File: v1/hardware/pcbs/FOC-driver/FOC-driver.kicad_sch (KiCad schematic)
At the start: 146 parts, among them J10 S4B-XH-A, J11 S10B-XH-A, J12 S8B-XH-A, J13 S5B-XH-A, J14 S2B-XH-A, J15 S5B-XH-A, J16 S2B-XH-A, J2 HB9500-3, J3 B2B-XH-A, J4 B2B-XH-A, J5 B2B-XH-A, J6 B2B-XH-A, J7 S2B-XH-A, J8 S5B-XH-A, J9 S4B-XH-A, Q10 40N05, Q11 40N05, Q8 40N05, Q9 40N05, SW1 TS-1088-AR02016, SW2 MSK22D18G2 125, Y1 C19674287, Y2 C48615

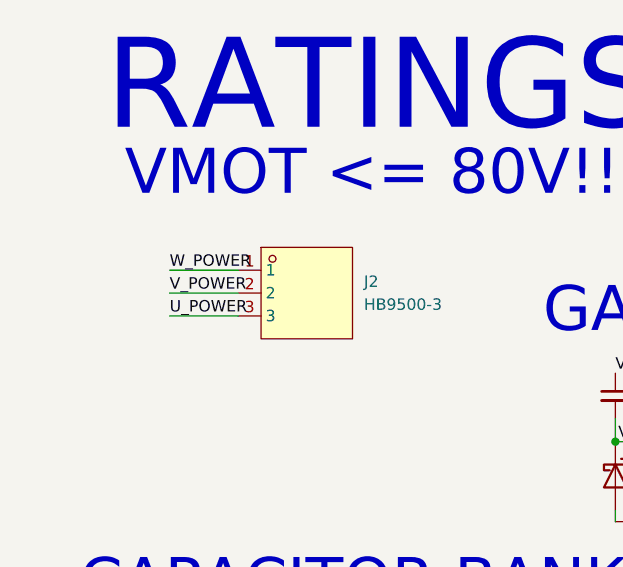
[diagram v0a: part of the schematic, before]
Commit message: new FOC driver inverter out label
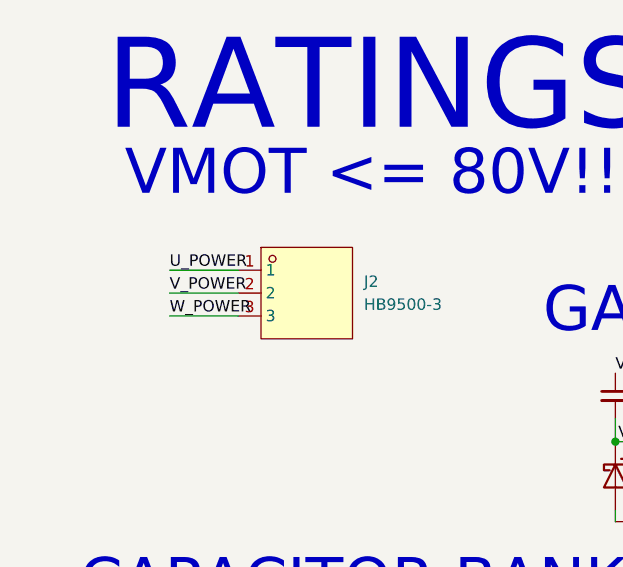
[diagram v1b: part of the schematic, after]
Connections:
- net U_POWER: now also J2.1; no longer J2.3
- net W_POWER: now also J2.3; no longer J2.1
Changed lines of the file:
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@@
 	(wire
 		(pts
+			(xy 24.13 53.34) (xy 31.75 53.34)
+		)
+		(stroke
+			(width 0)
+			(type default)
+		)
+	)
+	(wire
+		(pts
 			(xy 416.56 281.94) (xy 416.56 287.02)
 		)
@@
 	(wire
 		(pts
-			(xy 24.13 48.26) (xy 31.75 48.26)
-		)
-		(stroke
-			(width 0)
-			(type default)
-		)
-	)
-	(wire
-		(pts
 			(xy 466.09 48.26) (xy 463.55 48.26)
 		)
@@
 	(wire
 		(pts
+			(xy 24.13 48.26) (xy 31.75 48.26)
+		)
+		(stroke
+			(width 0)
+			(type default)
+		)
+	)
+	(wire
+		(pts
 			(xy 284.48 340.36) (xy 297.18 340.36)
 		)
@@
 		)
 	)
-	(wire
-		(pts
-			(xy 24.13 53.34) (xy 31.75 53.34)
-		)
-		(stroke
-			(width 0)
-			(type default)
-		)
-	)
 	(label "W_HIGH_GATE"
 		(at 191.77 91.44 0)
@@
 		)
 	)
+	(label "U_POWER"
+		(at 24.13 48.26 0)
+		(effects
+			(font
+				(size 1.27 1.27)
+			)
+			(justify left bottom)
+		)
+	)
 	(label "ENC_DIFF.B-"
 		(at 209.55 340.36 180)
@@
 		)
 	)
-	(label "W_POWER"
-		(at 24.13 48.26 0)
-		(effects
-			(font
-				(size 1.27 1.27)
-			)
-			(justify left bottom)
-		)
-	)
 	(label "ENC.A"
 		(at 430.53 95.25 0)
@@
 		)
 	)
-	(label "U_POWER"
-		(at 24.13 53.34 0)
-		(effects
-			(font
-				(size 1.27 1.27)
-			)
-			(justify left bottom)
-		)
-	)
 	(label "DEBUG{SWCLK SWDIO SWO}"
 		(at 387.35 134.62 180)
@@
 		)
 	)
+	(label "W_POWER"
+		(at 24.13 53.34 0)
+		(effects
+			(font
+				(size 1.27 1.27)
+			)
+			(justify left bottom)
+		)
+	)

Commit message: new FOC driver done
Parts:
- removed C31: 100nF 50V, Capacitor_SMD:C_0402_1005Metric, symbol symbols:C_Small
- removed C32: 1uF 16V, Capacitor_SMD:C_0402_1005Metric, symbol symbols:C_Small
- removed C4: 820uF 100V (C443165), Capacitor_THT:C_Radial_D18.0mm_H35.5mm_P7.50mm, symbol symbols:C_Polarized
- removed R4: 4.7K, Resistor_SMD:R_0402_1005Metric, symbol symbols:R_Small
- removed R5: 1K, Resistor_SMD:R_0402_1005Metric, symbol symbols:R_Small
- removed TH1, TH2, TH3, TH4, TH5, TH6: NCP15XH103F03RC, Resistor_SMD:R_0402_1005Metric, symbol Device:Thermistor
- removed TP17: TestPoint, Connector_PinSocket_2.54mm:PinSocket_1x01_P2.54mm_Vertical, symbol symbols:TestPoint
- added C70: 100nF 50V, Capacitor_SMD:C_0402_1005Metric, symbol symbols:C_Small
- added J17, J18, J19, J20, J21, J22: B2B-XH-A, Connector_JST:JST_XH_B2B-XH-A_1x02_P2.50mm_Vertical, symbol Connector_Generic:Conn_01x02
- added R68, R69, R70, R71, R72, R73, R74: 10K, Resistor_SMD:R_0402_1005Metric, symbol symbols:R_Small
- added R75, R76: 100, Resistor_SMD:R_0402_1005Metric, symbol symbols:R_Small
- added TP8: PinHeader 1x1, Connector_PinHeader_2.54mm:PinHeader_1x01_P2.54mm_Vertical, symbol symbols:TestPoint
- TP1, TP2, TP3, TP4, TP5, TP6, TP7: value TestPoint -> PinHeader 1x1; footprint Connector_PinSocket_2.54mm:PinSocket_1x01_P2.54mm_Vertical -> Connector_PinHeader_2.54mm:PinHeader_1x01_P2.54mm_Vertical
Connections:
- net 5V_SENSE is gone; now on net U_HIGH_TEMP: MCU1.13 (PA1)
- net VS1 is gone; now on net W_POWER: C9.1, GDRV1.18 (VS1)
- net VS2 is gone; now on net V_POWER: C10.1, GDRV1.15 (VS2)
- net VS3 is gone; now on net U_POWER: C11.1, GDRV1.12 (VS3)
- net +12V: now also TP6.1, C70.2; no longer TP5.1
- net +3.3V: now also J17.1 (Pin_1), J18.1 (Pin_1), J19.1 (Pin_1), J20.1 (Pin_1), J21.1 (Pin_1), J22.1 (Pin_1), TP8.1
- net +5V: now also TP7.1
- net 12V_SENSE: now also MCU1.17 (PA3); no longer MCU1.12 (PA0)
- net DEBUG.SWDIO: now also J15.2 (Pin_2); no longer J15.4 (Pin_4)
- net DEBUG.SWO: now also J15.4 (Pin_4); no longer J15.5 (Pin_5)
- net DIP.CONF0: now also MCU1.54 (PC12); no longer MCU1.30 (PB10)
- net DIP.CONF1: now also MCU1.53 (PC11); no longer MCU1.33 (PB11)
- net DIP.CONF2: now also MCU1.52 (PC10); no longer MCU1.34 (PB12)
- net ENC.SCS: now also MCU1.26 (PB2); no longer MCU1.37 (PB15)
- net ENDSTOP1: now also MCU1.62 (PB9); no longer MCU1.8 (PC0)
- net ENDSTOP1+: now also R75.1
- net ENDSTOP1-: now also R75.2
- net ENDSTOP2: now also MCU1.8 (PC0); no longer MCU1.62 (PB9)
- net ENDSTOP2+: now also R76.1
- net ENDSTOP2-: now also R76.2
- net FAN1.EN: now also MCU1.37 (PB15); no longer MCU1.26 (PB2)
- net FAN1.PWM: now also MCU1.41 (PC9); no longer MCU1.51 (PA15)
- net FAN2.EN: now also MCU1.34 (PB12); no longer MCU1.54 (PC12)
- net FAN2.PWM: now also MCU1.40 (PC8); no longer MCU1.39 (PC7)
- net FAN3.EN: now also MCU1.33 (PB11); no longer MCU1.53 (PC11)
- net FAN3.PWM: now also MCU1.39 (PC7); no longer MCU1.40 (PC8)
- net FAN4.EN: now also MCU1.30 (PB10); no longer MCU1.52 (PC10)
- net FAN4.PWM: now also MCU1.51 (PA15); no longer MCU1.41 (PC9)
- net FDCAN.CAN+: now also J8.3 (Pin_3), J8.4 (Pin_4), SW2.3; no longer J8.2 (Pin_2), J8.5 (Pin_5), SW2.2
- net FDCAN.CAN-: now also J8.2 (Pin_2), J8.5 (Pin_5), SW2.6; no longer J8.3 (Pin_3), J8.4 (Pin_4), SW2.5
- net GND: now also SW2.1, SW2.4, C70.1, R68.2, R69.2, R70.2, R71.2, R72.2, R73.2, R74.2; no longer TP7.1
- net MOTOR_TEMP: now also MCU1.20 (PA6)
- net NRST: now also J15.5 (Pin_5); no longer J15.2 (Pin_2)
- net RS422.RX+: now also J13.3 (Pin_3); no longer J13.4 (Pin_4)
- net RS422.RX-: now also J13.2 (Pin_2); no longer J13.5 (Pin_5)
- net RS422.TX+: now also J13.5 (Pin_5); no longer J13.2 (Pin_2)
- net RS422.TX-: now also J13.4 (Pin_4); no longer J13.3 (Pin_3)
- net U_HIGH_GATE: now also GDRV1.13 (HO3); no longer GDRV1.19 (HO1)
- net U_HIGH_PWM: now also GDRV1.24 (HIN3), MCU1.44 (PA10); no longer GDRV1.22 (HIN1), MCU1.42 (PA8)
- net U_HIGH_TEMP: now also J17.2 (Pin_2); no longer MCU1.14 (PA2)
- net U_LOW_GATE: now also GDRV1.9 (LO3); no longer GDRV1.11 (LO1)
- net U_LOW_PWM: now also GDRV1.3 (LIN3), MCU1.25 (PB1); no longer GDRV1.1 (LIN1), MCU1.2 (PC13)
- net U_LOW_TEMP: now also MCU1.14 (PA2), J18.2 (Pin_2); no longer MCU1.17 (PA3)
- net VMOT: now also TP5.1; no longer TP6.1
- net VMOT_SENSE: now also MCU1.22 (PC4); no longer MCU1.20 (PA6)
- net V_HIGH_TEMP: now also MCU1.11 (PC3), J19.2 (Pin_2); no longer MCU1.9 (PC1)
- net V_LOW_TEMP: now also MCU1.12 (PA0), J20.2 (Pin_2); no longer MCU1.10 (PC2)
- net W_HIGH_GATE: now also GDRV1.19 (HO1); no longer GDRV1.13 (HO3)
- net W_HIGH_PWM: now also GDRV1.22 (HIN1), MCU1.42 (PA8); no longer GDRV1.24 (HIN3), MCU1.44 (PA10)
- net W_HIGH_TEMP: now also MCU1.9 (PC1), J21.2 (Pin_2); no longer MCU1.11 (PC3)
- net W_LOW_GATE: now also GDRV1.11 (LO1); no longer GDRV1.9 (LO3)
- net W_LOW_PWM: now also GDRV1.1 (LIN1), MCU1.2 (PC13); no longer GDRV1.3 (LIN3), MCU1.25 (PB1)
- net W_LOW_TEMP: now also MCU1.10 (PC2), J22.2 (Pin_2); no longer MCU1.22 (PC4)
- net CANTERM_MID: now reaches C41.2, R35.1, R36.1
- net CANTERM+: now reaches R35.2
- net CANTERM+: now also SW2.2; no longer SW2.6
- net at DIFF_RECV1.4 (DI): now also R70.1
- net at DIFF_RECV6.4 (DI): now also R73.1
- net at DIFF_RECV2.4 (DI): now also R71.1
- net at DIFF_RECV4.4 (DI): now also R72.1
- net at DIFF_RECV5.4 (DI): now also R68.1
- net at DIFF_RECV7.4 (DI): now also R74.1
- net CANTERM-: now reaches R36.2
- net CANTERM-: now also SW2.5; no longer SW2.3
- net at DIFF_RECV3.4 (DI): now also R69.1
- no-connect marks 24 -> 15
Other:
- note added: "INVERTER: U_HIGH_PWM: TIM1_CH3 (PA10)r U_LOW_PWM: TIM1_CH3N (PB1) W_HIGH_PWM: TIM1_CH1 (PA8) W_LOW_PWM: TIM1_CH1N (PC13) V_HIGH_PWM: TIM1_CH2 (PA9) V_LOW_PWM: TIM1_CH2N (PB0) CURRENT SENSING: U_I_SENSE: OPAMP1_VINP => ADC1_IN13 (PA7) V_I_SENSE: OPAMP2_VINP => ADC2_IN16 (PB14) W_I_SENSE: OPAMP3_VINP => ADC1_IN12 (PB13) VOLTAGE SENSING: VMOT_SENSE: ADC2_IN5 (PC4) 12V_SENSE: ADC1_IN4 (PA3) TEMPERATU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"
- note added: "TESTPOINTS"
- note removed: "INVERTER: U_HIGH_PWM: TIM1_CH1 (PA8) U_LOW_PWM: TIM1_CH1N (PC13) V_HIGH_PWM: TIM1_CH2 (PA9) V_LOW_PWM: TIM1_CH2N (PB0) W_HIGH_PWM: TIM1_CH3 (PA10) W_LOW_PWM: TIM1_CH3N (PB1) CURRENT SENSING: U_I_SENSE: OPAMP1_VINP => ADC1_IN13 (PA7) V_I_SENSE: OPAMP2_VINP => ADC2_IN16 (PB14) W_I_SENSE: OPAMP3_VINP => ADC1_IN12 (PB13) VOLTAGE SENSING: VMOT_SENSE: ADC2_IN3 (PA6) 12V_SENSE: ADC1_IN1 (PA0) 5V_SENSE: 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"
- moved on the sheet: C10, C11, C17, C39, C41, C9, D1, D2, D3, FDCAN_TSCV1, J10, J8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

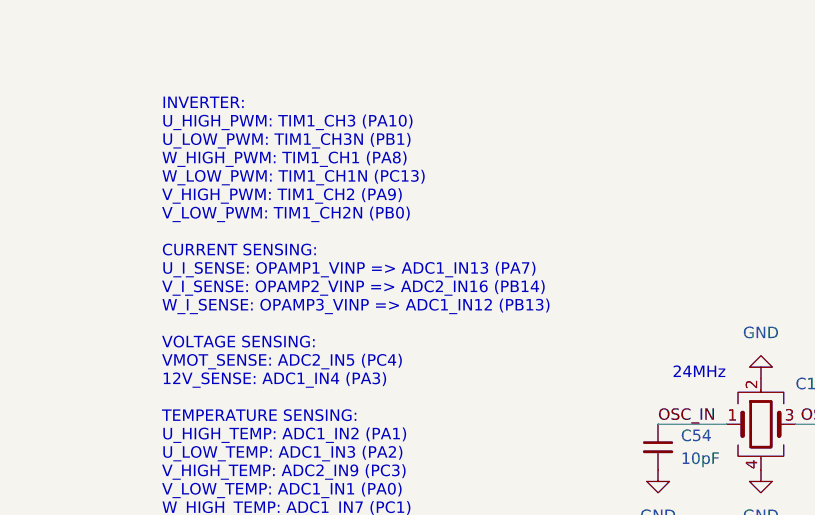
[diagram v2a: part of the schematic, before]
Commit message: corrected some pinouts
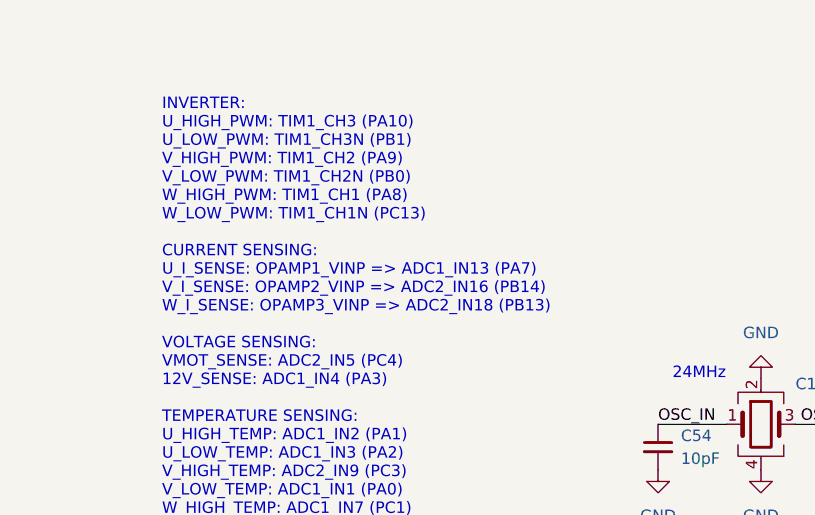
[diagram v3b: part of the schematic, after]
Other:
- note added: "INVERTER: U_HIGH_PWM: TIM1_CH3 (PA10)r U_LOW_PWM: TIM1_CH3N (PB1) V_HIGH_PWM: TIM1_CH2 (PA9)r V_LOW_PWM: TIM1_CH2N (PB0) W_HIGH_PWM: TIM1_CH1 (PA8) W_LOW_PWM: TIM1_CH1N (PC13) CURRENT SENSING: U_I_SENSE: OPAMP1_VINP => ADC1_IN13 (PA7) V_I_SENSE: OPAMP2_VINP => ADC2_IN16 (PB14) W_I_SENSE: OPAMP3_VINP => ADC2_IN18 (PB13) VOLTAGE SENSING: VMOT_SENSE: ADC2_IN5 (PC4) 12V_SENSE: ADC1_IN4 (PA3) TEMPERAT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"
- note removed: "INVERTER: U_HIGH_PWM: TIM1_CH3 (PA10)r U_LOW_PWM: TIM1_CH3N (PB1) W_HIGH_PWM: TIM1_CH1 (PA8) W_LOW_PWM: TIM1_CH1N (PC13) V_HIGH_PWM: TIM1_CH2 (PA9) V_LOW_PWM: TIM1_CH2N (PB0) CURRENT SENSING: U_I_SENSE: OPAMP1_VINP => ADC1_IN13 (PA7) V_I_SENSE: OPAMP2_VINP => ADC2_IN16 (PB14) W_I_SENSE: OPAMP3_VINP => ADC1_IN12 (PB13) VOLTAGE SENSING: VMOT_SENSE: ADC2_IN5 (PC4) 12V_SENSE: ADC1_IN4 (PA3) TEMPERATU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"
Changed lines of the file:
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@@
 		)
 	)
-	(text "INVERTER:\nU_HIGH_PWM: TIM1_CH3 (PA10)\r\nU_LOW_PWM: TIM1_CH3N (PB1)\nW_HIGH_PWM: TIM1_CH1 (PA8)\nW_LOW_PWM: TIM1_CH1N (PC13)\nV_HIGH_PWM: TIM1_CH2 (PA9)\nV_LOW_PWM: TIM1_CH2N (PB0)\n\nCURRENT SENSING:\nU_I_SENSE: OPAMP1_VINP => ADC1_IN13 (PA7)\nV_I_SENSE: OPAMP2_VINP => ADC2_IN16 (PB14)\nW_I_SENSE: OPAMP3_VINP => ADC1_IN12 (PB13)\n\nVOLTAGE SENSING:\nVMOT_SENSE: ADC2_IN5 (PC4)\n12V_SENSE: ADC1_IN4 (PA3)\n\nTEMPERATURE SENSING:\nU_HIGH_TEMP: ADC1_IN2 (PA1)\nU_LOW_TEMP: ADC1_IN3 (PA2)\nV_HIGH_TEMP: ADC2_IN9 (PC3)\nV_LOW_TEMP: ADC1_IN1 (PA0)\nW_HIGH_TEMP: ADC1_IN7 (PC1)\nW_LOW_TEMP: ADC1_IN8 (PC2)\nMOTOR_TEMP: ADC2_IN3 (PA6)\n\nFANS:\nFAN1_PWM: TIM8_CH4 (PC9)\r\nFAN1_EN: PB15\r\nFAN2_PWM: TIM8_CH3 (PC8)\r\nFAN2_EN: PB12\r\nFAN3_PWM: TIM8_CH2 (PC7)\r\nFAN3_EN: PB11\nFAN4_PWM: TIM8_CH1 (PA15)\nFAN4_EN: PB10\n\nDEBUG:\nSWCLK: PA14\nSWDIO: PA13\nSWO: PB3\nLED: PD2\n\nFDCAN:\nRX: FDCAN1_RX (PA11)\nTX: FDCAN1_TX (PA12)\n\nRS422:\nRX: USART1_RX (PB7)\nTX: USART1_TX (PB6)\n\nENCODER:\nSCLK: SPI1_SCLK (PA5)\nMISO: SPI1_MISO (PB4)\r\nMOSI: SPI1_MOSI (PB5)\nSCS: PB2\nA: TIM3_CH1 (PC6)\nB: TIM3_CH2 (PA4)\nZ: PC5\n\nENDSTOP:\nENDSTOP1: PB9\nENDSTOP2: PC0\n\nCONFIG:\nBOOT: BOOT0 (PB8)\nCONF1: PC12\nCONF2: PC11\nCONF3: PC10"
+	(text "INVERTER:\nU_HIGH_PWM: TIM1_CH3 (PA10)\r\nU_LOW_PWM: TIM1_CH3N (PB1)\nV_HIGH_PWM: TIM1_CH2 (PA9)\r\nV_LOW_PWM: TIM1_CH2N (PB0)\nW_HIGH_PWM: TIM1_CH1 (PA8)\nW_LOW_PWM: TIM1_CH1N (PC13)\n\nCURRENT SENSING:\nU_I_SENSE: OPAMP1_VINP => ADC1_IN13 (PA7)\nV_I_SENSE: OPAMP2_VINP => ADC2_IN16 (PB14)\nW_I_SENSE: OPAMP3_VINP => ADC2_IN18 (PB13)\n\nVOLTAGE SENSING:\nVMOT_SENSE: ADC2_IN5 (PC4)\n12V_SENSE: ADC1_IN4 (PA3)\n\nTEMPERATURE SENSING:\nU_HIGH_TEMP: ADC1_IN2 (PA1)\nU_LOW_TEMP: ADC1_IN3 (PA2)\nV_HIGH_TEMP: ADC2_IN9 (PC3)\nV_LOW_TEMP: ADC1_IN1 (PA0)\nW_HIGH_TEMP: ADC1_IN7 (PC1)\nW_LOW_TEMP: ADC1_IN8 (PC2)\nMOTOR_TEMP: ADC2_IN3 (PA6)\n\nFANS:\nFAN1_PWM: TIM8_CH4 (PC9)\r\nFAN1_EN: PB15\r\nFAN2_PWM: TIM8_CH3 (PC8)\r\nFAN2_EN: PB12\r\nFAN3_PWM: TIM8_CH2 (PC7)\r\nFAN3_EN: PB11\nFAN4_PWM: TIM8_CH1 (PA15)\nFAN4_EN: PB10\n\nDEBUG:\nSWCLK: PA14\nSWDIO: PA13\nSWO: PB3\nLED: PD2\n\nFDCAN:\nRX: FDCAN1_RX (PA11)\nTX: FDCAN1_TX (PA12)\n\nRS422:\nRX: USART1_RX (PB7)\nTX: USART1_TX (PB6)\n\nENCODER:\nSCLK: SPI1_SCLK (PA5)\nMISO: SPI1_MISO (PB4)\r\nMOSI: SPI1_MOSI (PB5)\nSCS: PB2\nA: TIM3_CH1 (PC6)\nB: TIM3_CH2 (PA4)\nZ: PC5\n\nENDSTOP:\nENDSTOP1: PB9\nENDSTOP2: PC0\n\nCONFIG:\nBOOT: BOOT0 (PB8)\nCONF1: PC12\nCONF2: PC11\nCONF3: PC10"
 		(exclude_from_sim no)
 		(at 308.102 92.71 0)
